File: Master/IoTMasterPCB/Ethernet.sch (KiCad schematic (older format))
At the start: 0 parts

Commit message: Finished RFID module sans antenna footprint. Added KSZ8081MNX and hierarchial connections.
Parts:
- added U?: KSZ8081MNX, Personal_ICs:KSZ8081MNX, symbol Personal_ICs:KSZ8081MNX
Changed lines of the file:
@@
 Comment4 ""
 $EndDescr
+$Comp
+L Personal_ICs:KSZ8081MNX U?
+U 1 1 5FF0DFBB
+P 4700 3050
+F 0 "U?" H 6744 2746 50  0000 L CNN
+F 1 "KSZ8081MNX" H 6744 2655 50  0000 L CNN
+F 2 "Personal_ICs:KSZ8081MNX" H 6550 3850 50  0001 L CNN
+F 3 "https://componentsearchengine.com/Datasheets/1/KSZ8081MNXIA-TR.pdf" H 6550 3750 50  0001 L CNN
+	1    4700 3050
+	1    0    0    -1
+$EndComp
 $EndSCHEMATC

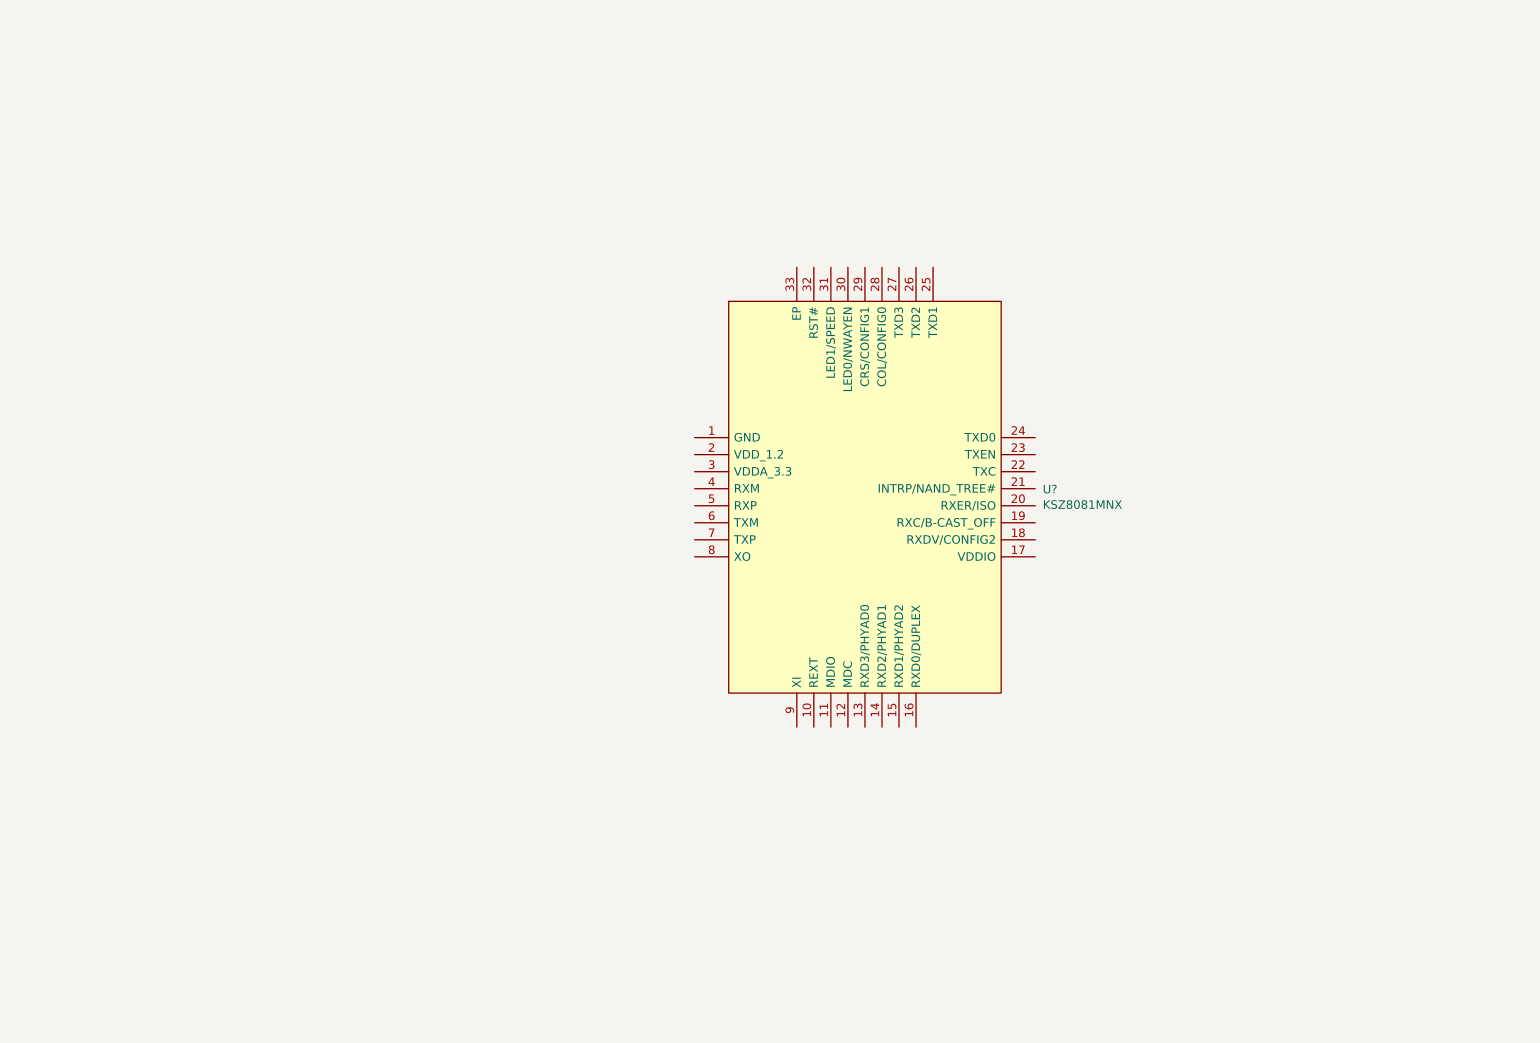
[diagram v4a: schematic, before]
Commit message: Finished RFID and Ethernet circuits.
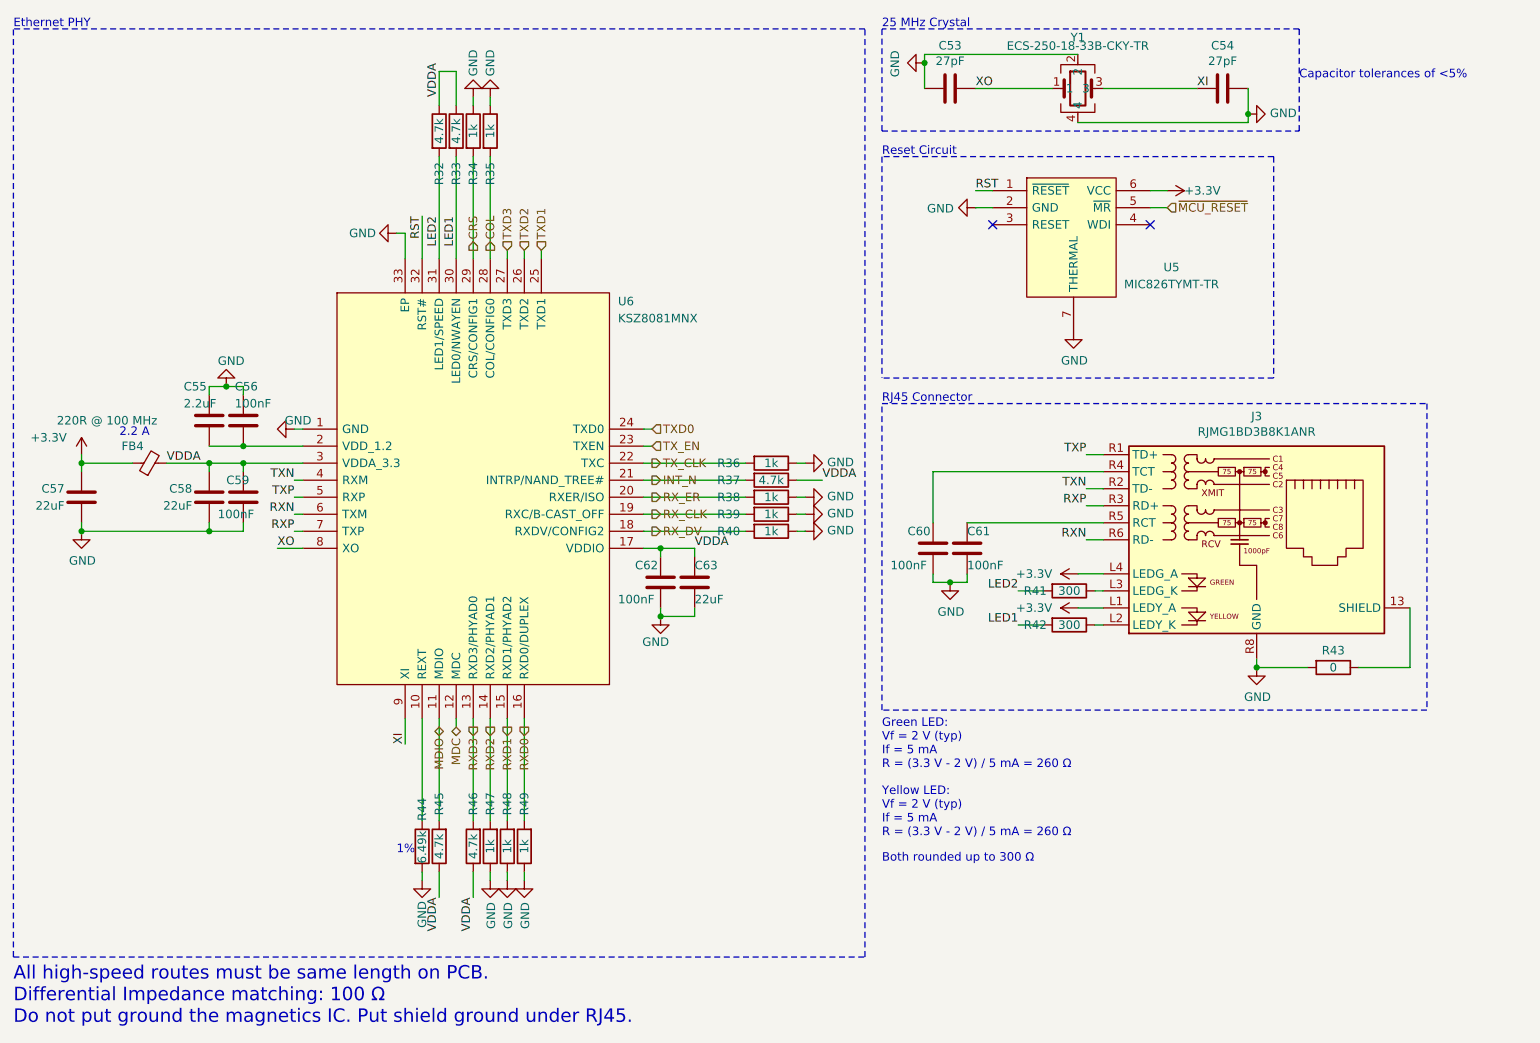
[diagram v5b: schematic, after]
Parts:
- added C53, C54: 27pF, Capacitor_SMD:C_0603_1608Metric, symbol Device:C
- added C55: 2.2uF, Capacitor_SMD:C_0603_1608Metric, symbol Device:C
- added C56, C59, C60, C61, C62: 100nF, Capacitor_SMD:C_0603_1608Metric, symbol Device:C
- added C57, C58: 22uF, Capacitor_SMD:C_1206_3216Metric, symbol Device:C
- added C63: 22uF, Capacitor_SMD:C_0603_1608Metric, symbol Device:C
- added FB4: 220R @ 100 MHz, Inductor_SMD:L_0603_1608Metric, symbol Device:Ferrite_Bead_Small
- added J3: RJMG1BD3B8K1ANR, Connector_RJ:RJ45_Amphenol_RJMG1BD3B8K1ANR, symbol Connector:RJ45_Amphenol_RJMG1BD3B8K1ANR
- added R32, R33, R37, R45, R46: 4.7k, Resistor_SMD:R_0603_1608Metric, symbol Device:R
- added R34, R35, R36, R38, R39, R40, R47, R48, R49: 1k, Resistor_SMD:R_0603_1608Metric, symbol Device:R
- added R41, R42: 300, Resistor_SMD:R_0603_1608Metric, symbol Device:R
- added R43: 0, Resistor_SMD:R_1206_3216Metric, symbol Device:R
- added R44: 6.49k, Resistor_SMD:R_0603_1608Metric, symbol Device:R
- added U5: MIC826TYMT-TR, Vikings_devices:MIC826TYMT-TR, symbol Vikings_actives:MIC826TYMT-TR
- added Y1: ECS-250-18-33B-CKY-TR, Vikings_devices:ECS-250-18-33B-CKY, symbol Vikings_actives:ECS-250-18-33B-CKY-TR
- gave numbers to parts that had none: 1
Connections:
- net GND: now reaches U6.1 (GND)
- net GND: now also U6.33 (EP), C53.2, C54.2, C55.1, C56.1, C57.1, C58.1, C59.2, C60.2, C61.2, C62.2, C63.2, J3.R8 (GND), R34.1, R35.1, R36.1, R38.1, R39.1, R40.1, R43.2, R44.2, R47.1, R48.1, R49.1, U5.2 (GND), U5.7 (THERMAL), Y1.2, Y1.4
- net at U6.10 (REXT): now also R44.1
- net MDIO: now reaches U6.11 (MDIO)
- net MDIO: now also R45.2
- net MDC: now reaches U6.12 (MDC)
- net RXD3: now reaches U6.13 (RXD3/PHYAD0)
- net RXD3: now also R46.2
- net RXD2: now reaches U6.14 (RXD2/PHYAD1)
- net RXD2: now also R47.2
- net RXD1: now reaches U6.15 (RXD1/PHYAD2)
- net RXD1: now also R48.2
- net RXD0: now reaches U6.16 (RXD0/DUPLEX)
- net RXD0: now also R49.2
- net VDDA: now reaches U6.17 (VDDIO)
- net VDDA: now also U6.3 (VDDA_3.3), C58.2, C59.1, C62.1, C63.1, FB4.2, R32.1, R33.1, R37.1, R45.1, R46.1
- net RX_DV: now reaches U6.18 (RXDV/CONFIG2)
- net RX_DV: now also R40.2
- net RX_CLK: now reaches U6.19 (RXC/B-CAST_OFF)
- net RX_CLK: now also R39.2
- net at U6.2 (VDD_1.2): now also C55.2, C56.2
- net RX_ER: now reaches U6.20 (RXER/ISO)
- net RX_ER: now also R38.2
- net INT_N: now reaches U6.21 (INTRP/NAND_TREE#)
- net INT_N: now also R37.2
- net TX_CLK: now reaches U6.22 (TXC)
- net TX_CLK: now also R36.2
- net TX_EN: now reaches U6.23 (TXEN)
- net TXD0: now reaches U6.24 (TXD0)
- net TXD1: now reaches U6.25 (TXD1)
- net TXD2: now reaches U6.26 (TXD2)
- net TXD3: now reaches U6.27 (TXD3)
- net COL: now reaches U6.28 (COL/CONFIG0)
- net COL: now also R35.2
- net CRS: now reaches U6.29 (CRS/CONFIG1)
- net CRS: now also R34.2
- net LED1: now reaches U6.30 (LED0/NWAYEN)
- net LED1: now also R33.2, R42.2
- net LED2: now reaches U6.31 (LED1/SPEED)
- net LED2: now also R32.2, R41.2
- net RST: now reaches U6.32 (RST#)
- net RST: now also U5.1 (~RESET)
- net TXN: now reaches U6.4 (RXM)
- net TXN: now also J3.R2 (TD-)
- net TXP: now reaches U6.5 (RXP)
- net TXP: now also J3.R1 (TD+)
- net RXN: now reaches U6.6 (TXM)
- net RXN: now also J3.R6 (RD-)
- net RXP: now reaches U6.7 (TXP)
- net RXP: now also J3.R3 (RD+)
- net XO: now reaches U6.8 (XO)
- net XO: now also C53.1, Y1.1
- net XI: now reaches U6.9 (XI)
- net XI: now also C54.1, Y1.3
- new net: J3.13 (SHIELD), R43.1
- new net: J3.L2 (LEDY_K), R42.1
- new net: J3.L3 (LEDG_K), R41.1
- new net: C60.1, J3.R4 (TCT)
- new net: C61.1, J3.R5 (RCT)
- new net +3V3: C57.2, FB4.1, J3.L1 (LEDY_A), J3.L4 (LEDG_A), U5.6 (VCC)
- new net ~MCU_RESET: U5.5 (~MR)
- no-connect marks 0 -> 2
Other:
- note added: "1%"
- note added: "2.2 A"
- note added: "25 MHz Crystal"
- note added: "All high-speed routes must be same length on PCB.\nDifferential Impedance matching: 100 Ω\nDo not put ground the magnetics IC. Put shield ground under RJ45."
- note added: "Both rounded up to 300 Ω"
- note added: "Capacitor tolerances of <5%"
- note added: "Ethernet PHY"
- note added: "Green LED:\nVf = 2 V (typ)\nIf = 5 mA\nR = (3.3 V - 2 V) / 5 mA = 260 Ω"
- note added: "RJ45 Connector"
- note added: "Reset Circuit"
- note added: "Yellow LED:\nVf = 2 V (typ)\nIf = 5 mA\nR = (3.3 V - 2 V) / 5 mA = 260 Ω"
- moved on the sheet: U6

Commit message: Minor changes to schematic, finished placing all components, only minor fixes needed to PCB now.
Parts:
- removed J3: RJMG1BD3B8K1ANR, Connector_RJ:RJ45_Amphenol_RJMG1BD3B8K1ANR, symbol Connector:RJ45_Amphenol_RJMG1BD3B8K1ANR
- added J3: RJMG1BD3B8K1ANR, Personal_Misc:RJMG1BD3B8K1ANR, symbol Personal_Misc:RJMG1BD3B8K1ANR
- renumbered Y1 to X1
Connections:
- net +3V3: now also J3.L1 (LEDY_A), J3.L4 (LEDG_A)
- net GND: now also J3.R8 (GND)
- net RXN: now also J3.R6 (RD-)
- net RXP: now also J3.R3 (RD+)
- net TXN: now also J3.R2 (TD-)
- net TXP: now also J3.R1 (TD+)
- net at R43.1: now also J3.13 (SHIELD)
- net at R42.1: now also J3.L2 (LEDY_K)
- net at R41.1: now also J3.L3 (LEDG_K)
- net at C60.1: now also J3.R4 (TCT)
- net at C61.1: now also J3.R5 (RCT)
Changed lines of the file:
@@
 AR Path="/5FE33B68" Ref="Y?"  Part="1"
 AR Path="/5F5FC96C/5FE33B68" Ref="Y?"  Part="1"
-AR Path="/5F9EEF53/5FE33B68" Ref="Y1"  Part="1"
-F 0 "Y1" H 6950 1300 50  0000 C CNN
+AR Path="/5F9EEF53/5FE33B68" Ref="X1"  Part="1"
+F 0 "X1" H 6950 1300 50  0000 C CNN
 F 1 "ECS-250-18-33B-CKY-TR" H 6950 1250 50  0000 C CNN
 F 2 "Vikings_devices:ECS-250-18-33B-CKY" H 7400 1150 50  0001 L CNN
@@
 All high-speed routes must be same length on PCB.\nDifferential Impedance matching: 100 Ω\nDo not put ground the magnetics IC. Put shield ground under RJ45.
 $Comp
-L Connector:RJ45_Amphenol_RJMG1BD3B8K1ANR J3
-U 1 1 5FD36EA5
-P 8000 3650
-F 0 "J3" H 8000 4375 50  0000 C CNN
-F 1 "RJMG1BD3B8K1ANR" H 8000 4284 50  0000 C CNN
-F 2 "Connector_RJ:RJ45_Amphenol_RJMG1BD3B8K1ANR" H 8000 4350 50  0001 C CNN
-F 3 "https://www.amphenolcanada.com/ProductSearch/Drawings/AC/RJMG1BD3B8K1ANR.PDF" H 8000 4450 50  0001 C CNN
-	1    8000 3650
-	1    0    0    -1
-$EndComp
-$Comp
 L power:GND #PWR0170
 U 1 1 5FD3FA0F
@@
 Wire Notes Line
 	5700 650  700  650
+$Comp
+L Personal_Misc:RJMG1BD3B8K1ANR J3
+U 1 1 60131064
+P 8000 3650
+F 0 "J3" H 8000 4375 50  0000 C CNN
+F 1 "RJMG1BD3B8K1ANR" H 8000 4284 50  0000 C CNN
+F 2 "Personal_Misc:RJMG1BD3B8K1ANR" H 8000 4350 50  0001 C CNN
+F 3 "https://www.amphenolcanada.com/ProductSearch/Drawings/AC/RJMG1BD3B8K1ANR.PDF" H 8000 4450 50  0001 C CNN
+	1    8000 3650
+	1    0    0    -1
+$EndComp
 $EndSCHEMATC
